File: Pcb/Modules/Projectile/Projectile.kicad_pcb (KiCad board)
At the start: 2 copper layers, 55.2 x 20.2 mm, 18 parts, among them J1 Conn_01x02, J2 Conn_01x04, Q1 BC817, U1 OP249

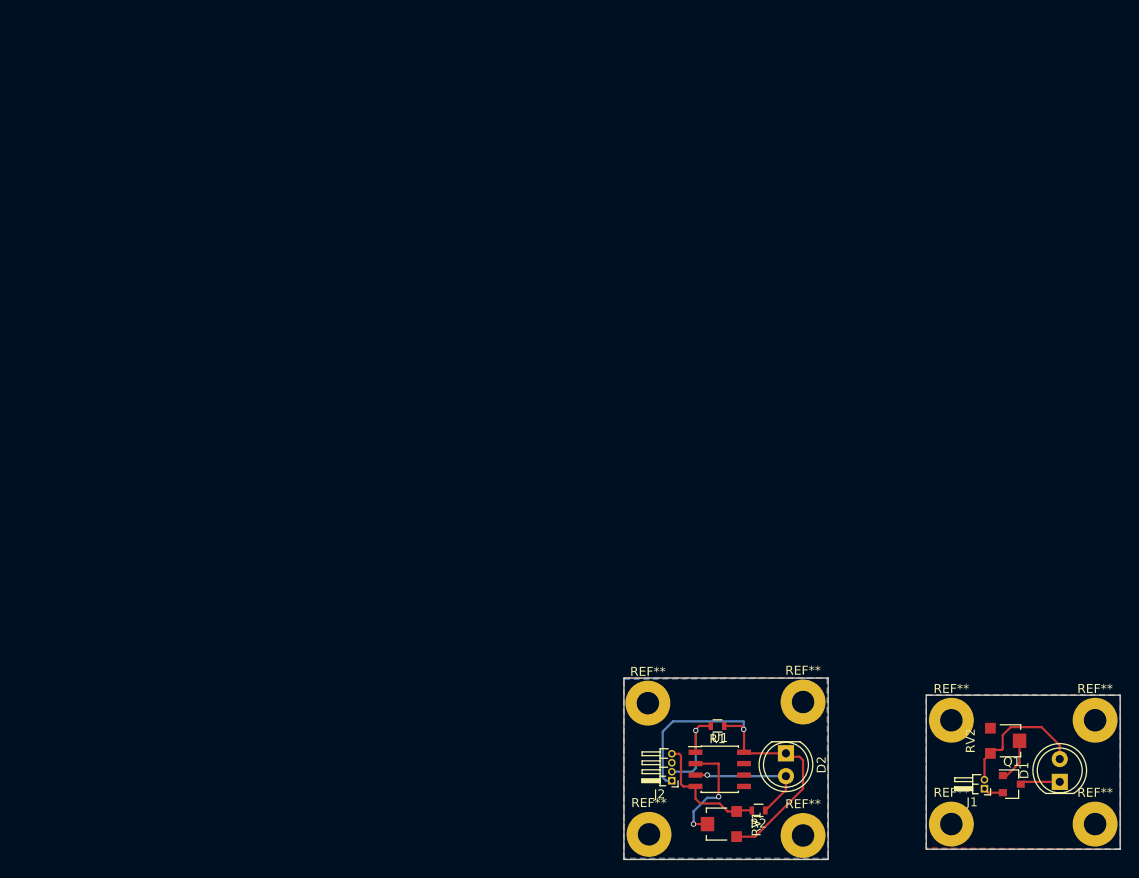
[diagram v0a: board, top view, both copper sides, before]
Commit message: Pcb layout for beam and projectile module
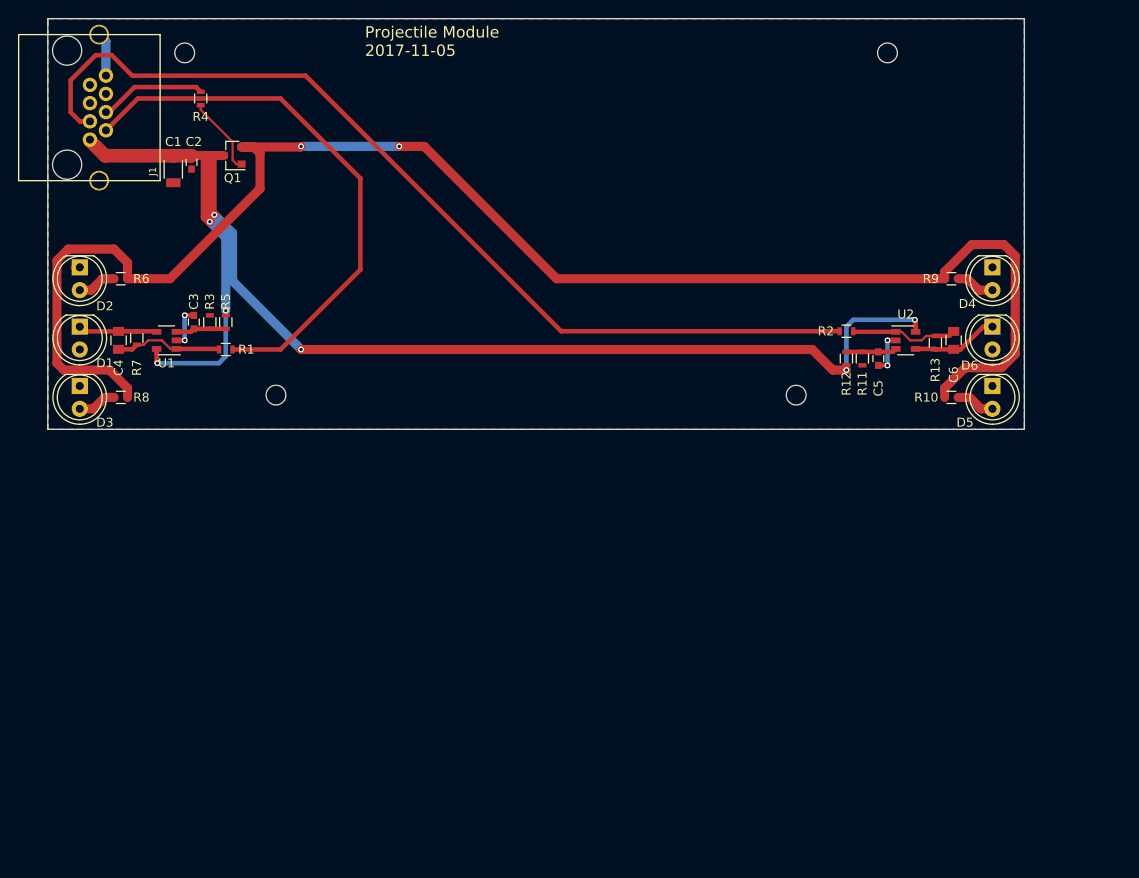
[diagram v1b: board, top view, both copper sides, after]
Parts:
- removed J2: Conn_01x04, Pin_Headers:Pin_Header_Angled_1x04_Pitch1.00mm
- removed REF** (x8): MountingHole_2.5mm_Pad, Mounting_Holes:MountingHole_2.5mm_Pad
- removed RV1, RV2: POT, Potentiometers:Potentiometer_Trimmer-EVM3E
- added C1: 10uF, Capacitors_SMD:C_1206, F.Cu at (43.2, 40.9)
- added C2: 0.1uF, Capacitors_SMD:C_0603, F.Cu at (45.2, 40.1)
- added C3: 1uF, Capacitors_SMD:C_0603, F.Cu at (45.5, 57.9)
- added C4: 4.3pF, Capacitors_SMD:C_0805, F.Cu at (37.1, 59.9)
- added C5: 1uF, Capacitors_SMD:C_0603, F.Cu at (121.7, 62.0)
- added C6: 4.3pF, Capacitors_SMD:C_0805, F.Cu at (130.0, 59.9)
- added D3: LED, LEDs:LED_D5.0mm, F.Cu at (32.8, 65.0)
- added D4: LED, LEDs:LED_D5.0mm, F.Cu at (134.4, 51.8)
- added D5: LED, LEDs:LED_D5.0mm, F.Cu at (134.4, 65.0)
- added D6: D_Photo, LEDs:LED_D5.0mm, F.Cu at (134.4, 58.4)
- added R10: 30R, Resistors_SMD:R_0603, F.Cu at (129.8, 66.3)
- added R11: 8.98K, Resistors_SMD:R_0603, F.Cu at (119.9, 62.0)
- added R12: 280R, Resistors_SMD:R_0603, F.Cu at (118.1, 62.0)
- added R13: 34.8K, Resistors_SMD:R_0603, F.Cu at (128.0, 60.2)
- added R3: 8.98K, Resistors_SMD:R_0603, F.Cu at (47.2, 57.9)
- added R4: 1K, Resistors_SMD:R_0603, F.Cu at (46.2, 33.0)
- added R5: 280R, Resistors_SMD:R_0603, F.Cu at (49.0, 57.9)
- added R6: 30R, Resistors_SMD:R_0603, F.Cu at (37.3, 53.1)
- added R7: 34.8K, Resistors_SMD:R_0603, F.Cu at (39.1, 59.7)
- added R8: 30R, Resistors_SMD:R_0603, F.Cu at (37.3, 66.3)
- added R9: 30R, Resistors_SMD:R_0603, F.Cu at (129.8, 53.1)
- added U2: OPA320, TO_SOT_Packages_SMD:SOT-23-5, F.Cu at (124.7, 59.9)
- added X1: HOLE, Mounting_Holes:MountingHole_2.2mm_M2, F.Cu at (112.5, 66.0)
- added X2: HOLE, Mounting_Holes:MountingHole_2.2mm_M2, F.Cu at (54.6, 66.0)
- added X3: HOLE, Mounting_Holes:MountingHole_2.2mm_M2, F.Cu at (44.5, 27.9)
- added X4: HOLE, Mounting_Holes:MountingHole_2.2mm_M2, F.Cu at (122.7, 27.9)
- D1: value LD274 -> D_Photo
- D2: value LD274 -> LED
- J1: value Conn_01x02 -> JACK_RJ45; footprint Pin_Headers:Pin_Header_Angled_1x02_Pitch1.00mm -> CA6:RJ45_pcbwing
- Q1: value BC817 -> Q_NMOS_GSD
- R1, R2: value R -> 50R
- U1: value OP249 -> OPA320; footprint Housings_SOIC:SOIC-8_3.9x4.9mm_Pitch1.27mm -> TO_SOT_Packages_SMD:SOT-23-5
- moved J1 125.3 mm to (33.8, 34.0), turned to 270 degrees
- moved D1 120.3 mm to (32.8, 58.4), turned to 270 degrees
- moved Q1 111.4 mm to (49.8, 39.4), turned to 180 degrees
- moved D2 95.4 mm to (32.8, 51.8)
- moved U1 77.9 mm to (42.4, 59.9), turned to 180 degrees
- moved R1 68.9 mm to (49.0, 61.0), turned to 0 degrees
- moved R2 54.2 mm to (118.1, 58.9)
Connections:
- D1 pad 1: Net-(D1-Pad1) -> Net-(C4-Pad2)
- D1 pad 2: Net-(D1-Pad2) -> GND
- D2 pad 1: Net-(D2-Pad1) -> GND
- J1 pad 1: Net-(J1-Pad1) -> 3V3
- J1 pad 2: Net-(D1-Pad2) -> Net-(J1-Pad2)
- Q1 pad 2: Net-(J1-Pad1) -> Net-(Q1-Pad2)
- Q1 pad 3: Net-(D1-Pad1) -> 3V3
- R1 pad 1: Net-(D2-Pad1) -> Net-(C4-Pad1)
- R1 pad 2: Net-(J2-Pad2) -> Net-(J1-Pad2)
- R2 pad 1: Net-(D2-Pad2) -> Net-(C6-Pad1)
- R2 pad 2: Net-(J2-Pad4) -> Net-(J1-Pad3)
- U1 pad 1: Net-(J2-Pad2) -> Net-(C4-Pad1)
- U1 pad 2: Net-(RV1-Pad2) -> GND
- U1 pad 3: Net-(D2-Pad2) -> Net-(C3-Pad1)
- U1 pad 4: Net-(J2-Pad4) -> Net-(C4-Pad2)
- U1 pad 5: (no net) -> 3V3
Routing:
- net Net-(Q1-Pad2): track 0.00 -> 173.6 mm, vias 0 -> 2
- net 3V3: track 0.00 -> 151.1 mm, vias 0 -> 7
- net Net-(J1-Pad3): track 0.00 -> 105.6 mm
- net Net-(J1-Pad2): track 0.00 -> 61.6 mm
- net Net-(D2-Pad1): track 41.4 -> 0.00 mm, vias 1 -> 0
- net Net-(D1-Pad2): track 15.4 -> 0.00 mm
- net GND: track 0.00 -> 14.9 mm, vias 0 -> 4
- net Net-(J2-Pad4): track 14.3 -> 0.00 mm
- net Net-(RV1-Pad2): track 12.7 -> 0.00 mm, vias 2 -> 0
- net Net-(C6-Pad1): track 0.00 -> 12.0 mm
- net Net-(C4-Pad1): track 0.00 -> 12.0 mm
- net Net-(J1-Pad4): track 0.00 -> 11.9 mm
- net Net-(J2-Pad2): track 11.5 -> 0.00 mm, vias 1 -> 0
- net Net-(D2-Pad2): track 14.9 -> 4.35 mm, vias 1 -> 0
- net Net-(C6-Pad2): track 0.00 -> 9.62 mm
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- added copper zone on B.Cu, net GND
- added copper zone on F.Cu, net GND
- removed copper zone on B.Cu, net (none)
- removed copper zone on F.Cu, net (none)
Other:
- board size 55.2 x 20.2 mm -> 108.7 x 45.7 mm
- net class Default: clearance 0.2 -> 0.2032; trace_width 0.25 -> 0.254; via_dia 0.6 -> 0.6604; via_drill 0.4 -> 0.3556
- rule trace_clearance: 0.2 -> 0.2032
- board text added: "Projectile Module 2017-11-05"

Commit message: Change 50 ohm resistor to 49.9
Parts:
- R1, R2: value 50R -> 49.9R
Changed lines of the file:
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@@
       (effects (font (size 1 1) (thickness 0.15)))
     )
-    (fp_text value 50R (at 0 1.5) (layer F.Fab) hide
+    (fp_text value 49.9R (at 0 1.5) (layer F.Fab) hide
       (effects (font (size 1 1) (thickness 0.15)))
     )
@@
       (effects (font (size 1 1) (thickness 0.15)))
     )
-    (fp_text value 50R (at 0 1.5 180) (layer F.Fab) hide
+    (fp_text value 49.9R (at 0 1.5 180) (layer F.Fab) hide
       (effects (font (size 1 1) (thickness 0.15)))
     )

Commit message: Update PCBs
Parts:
- added R14: 100K, Resistors_SMD:R_0603, F.Cu at (49.8, 42.7)
- J1: moved to B.Cu
- R10, R6, R8, R9: value 30R -> 49.9
- R11, R3: value 8.98K -> 280R
- R12, R5: value 280R -> 8.98K
- R13, R7: value 34.8K -> 100K
- X1, X2, X3, X4: footprint Mounting_Holes:MountingHole_2.2mm_M2 -> Mounting_Holes:MountingHole_2.5mm_Pad
- moved X4 10.3 mm to (112.4, 27.9)
- moved X3 10.2 mm to (54.6, 27.9)
- moved R4 4.05 mm to (48.9, 36.1), turned to 0 degrees
- moved X1 0.13 mm to (112.4, 66.0)
- turned J1 to 90 degrees
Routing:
- net 3V3: track 151.1 -> 162.3 mm
- net Net-(J1-Pad3): track 105.6 -> 101.4 mm, vias 0 -> 1
- net GND: track 14.9 -> 11.4 mm, vias 4 -> 5
- net Net-(J1-Pad4): track 11.9 -> 13.5 mm
- net Net-(Q1-Pad1): track 8.76 -> 7.18 mm
- net Net-(J1-Pad2): track 61.6 -> 60.7 mm
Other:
- board text added: "Projectile Module 2017-12-03"
- board text removed: "Projectile Module 2017-11-05"

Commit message: Update pcbs.
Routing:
- net GND: track 11.4 -> 17.2 mm, vias 5 -> 10
- removed copper zone on F.Cu, net GND
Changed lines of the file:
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@@
     (thickness 1.6)
     (drawings 5)
-    (tracks 167)
+    (tracks 179)
     (zones 0)
     (modules 34)
@@
   )
   (setup
-    (last_trace_width 0.508)
+    (last_trace_width 0.254)
     (user_trace_width 0.2032)
     (user_trace_width 0.254)
@@
       (effects (font (size 1 1) (thickness 0.15)))
     )
-    (fp_text value D_Photo (at 1.27 3.96 270) (layer F.Fab)
+    (fp_text value D_Photo (at 1.27 3.96 270) (layer F.Fab) hide
       (effects (font (size 1 1) (thickness 0.15)))
     )
@@
       (effects (font (size 1 1) (thickness 0.15)))
     )
-    (fp_text value LED (at 1.27 3.96 270) (layer F.Fab)
+    (fp_text value LED (at 1.27 3.96 270) (layer F.Fab) hide
       (effects (font (size 1 1) (thickness 0.15)))
     )
@@
       (effects (font (size 1 1) (thickness 0.15)))
     )
-    (fp_text value LED (at 1.27 3.96 270) (layer F.Fab)
+    (fp_text value LED (at 1.27 3.96 270) (layer F.Fab) hide
       (effects (font (size 1 1) (thickness 0.15)))
     )
@@
       (effects (font (size 1 1) (thickness 0.15)))
     )
-    (fp_text value LED (at 1.27 3.96 270) (layer F.Fab)
+    (fp_text value LED (at 1.27 3.96 270) (layer F.Fab) hide
       (effects (font (size 1 1) (thickness 0.15)))
     )
@@
       (effects (font (size 1 1) (thickness 0.15)))
     )
-    (fp_text value LED (at 1.27 3.96 270) (layer F.Fab)
+    (fp_text value LED (at 1.27 3.96 270) (layer F.Fab) hide
       (effects (font (size 1 1) (thickness 0.15)))
     )
@@
       (effects (font (size 1 1) (thickness 0.15)))
     )
-    (fp_text value D_Photo (at 1.27 3.96 270) (layer F.Fab)
+    (fp_text value D_Photo (at 1.27 3.96 270) (layer F.Fab) hide
       (effects (font (size 1 1) (thickness 0.15)))
     )
@@
       (effects (font (size 1 1) (thickness 0.15)))
     )
-    (fp_text value 49.9 (at 0 1.5) (layer F.Fab)
+    (fp_text value 49.9 (at 0 1.5) (layer F.Fab) hide
       (effects (font (size 1 1) (thickness 0.15)))
     )
@@
       (effects (font (size 1 1) (thickness 0.15)))
     )
-    (fp_text value 49.9 (at 0 1.5) (layer F.Fab)
+    (fp_text value 49.9 (at 0 1.5) (layer F.Fab) hide
       (effects (font (size 1 1) (thickness 0.15)))
     )
@@
       (effects (font (size 1 1) (thickness 0.15)))
     )
-    (fp_text value 49.9 (at 0 1.5 180) (layer F.Fab)
+    (fp_text value 49.9 (at 0 1.5 180) (layer F.Fab) hide
       (effects (font (size 1 1) (thickness 0.15)))
     )
@@
   (segment (start 41.318 62.4) (end 41.402 62.484) (width 0.508) (layer F.Cu) (net 1))
   (segment (start 41.318 60.894) (end 41.318 62.4) (width 0.508) (layer F.Cu) (net 1) (status 10))
-  (segment (start 49.034 42.672) (end 49.034 41.795) (width 0.508) (layer F.Cu) (net 2))
-  (via (at 48.641 41.402) (size 0.6604) (drill 0.3556) (layers F.Cu B.Cu) (net 2))
-  (segment (start 49.034 41.795) (end 48.641 41.402) (width 0.508) (layer F.Cu) (net 2))
+  (segment (start 43.18 42.394) (end 43.18 43.688) (width 1.016) (layer F.Cu) (net 2))
+  (via (at 43.18 43.688) (size 0.6604) (drill 0.3556) (layers F.Cu B.Cu) (net 2))
+  (segment (start 43.18 42.394) (end 41.426 42.394) (width 1.016) (layer F.Cu) (net 2))
+  (via (at 41.148 42.672) (size 0.6604) (drill 0.3556) (layers F.Cu B.Cu) (net 2))
+  (segment (start 41.426 42.394) (end 41.148 42.672) (width 1.016) (layer F.Cu) (net 2))
+  (segment (start 49.034 42.672) (end 49.034 41.668) (width 0.508) (layer F.Cu) (net 2))
+  (via (at 49.022 41.656) (size 0.6604) (drill 0.3556) (layers F.Cu B.Cu) (net 2))
+  (segment (start 49.034 41.668) (end 49.022 41.656) (width 0.508) (layer F.Cu) (net 2))
+  (segment (start 45.212 40.882) (end 45.212 41.91) (width 0.508) (layer F.Cu) (net 2))
+  (via (at 45.212 41.91) (size 0.6604) (drill 0.3556) (layers F.Cu B.Cu) (net 2))
+  (segment (start 47.244 57.162) (end 47.002 57.162) (width 0.508) (layer F.Cu) (net 2))
+  (segment (start 47.002 57.162) (end 46.482 56.642) (width 0.508) (layer F.Cu) (net 2))
+  (via (at 46.482 56.642) (size 0.6604) (drill 0.3556) (layers F.Cu B.Cu) (net 2))
+  (segment (start 119.888 62.726) (end 119.888 63.5) (width 0.508) (layer F.Cu) (net 2))
+  (via (at 119.888 63.5) (size 0.6604) (drill 0.3556) (layers F.Cu B.Cu) (net 2))
   (segment (start 123.614 59.944) (end 122.682 59.944) (width 0.508) (layer F.Cu) (net 2) (status 10))
   (segment (start 122.67 62.726) (end 121.666 62.726) (width 0.508) (layer F.Cu) (net 2) (status 20))
@@
   (segment (start 52.832 43.053) (end 52.832 39.116) (width 1.016) (layer F.Cu) (net 17))
   (segment (start 42.799 53.086) (end 52.832 43.053) (width 1.016) (layer F.Cu) (net 17))
-  (zone (net 2) (net_name GND) (layer F.Cu) (hatch edge 0.508)
-    (connect_pads (clearance 0.254))
-    (min_thickness 0.3048)
-    (fill yes (arc_segments 16) (thermal_gap 0.1524) (thermal_bridge_width 0.381))
-    (polygon
-      (pts
-        (xy 137.922 69.85) (xy 29.21 69.85) (xy 29.21 24.13) (xy 137.922 24.13)
-      )
-    )
-  )
   (zone (net 2) (net_name GND) (layer B.Cu) (hatch edge 0.508)
     (connect_pads (clearance 0.254))

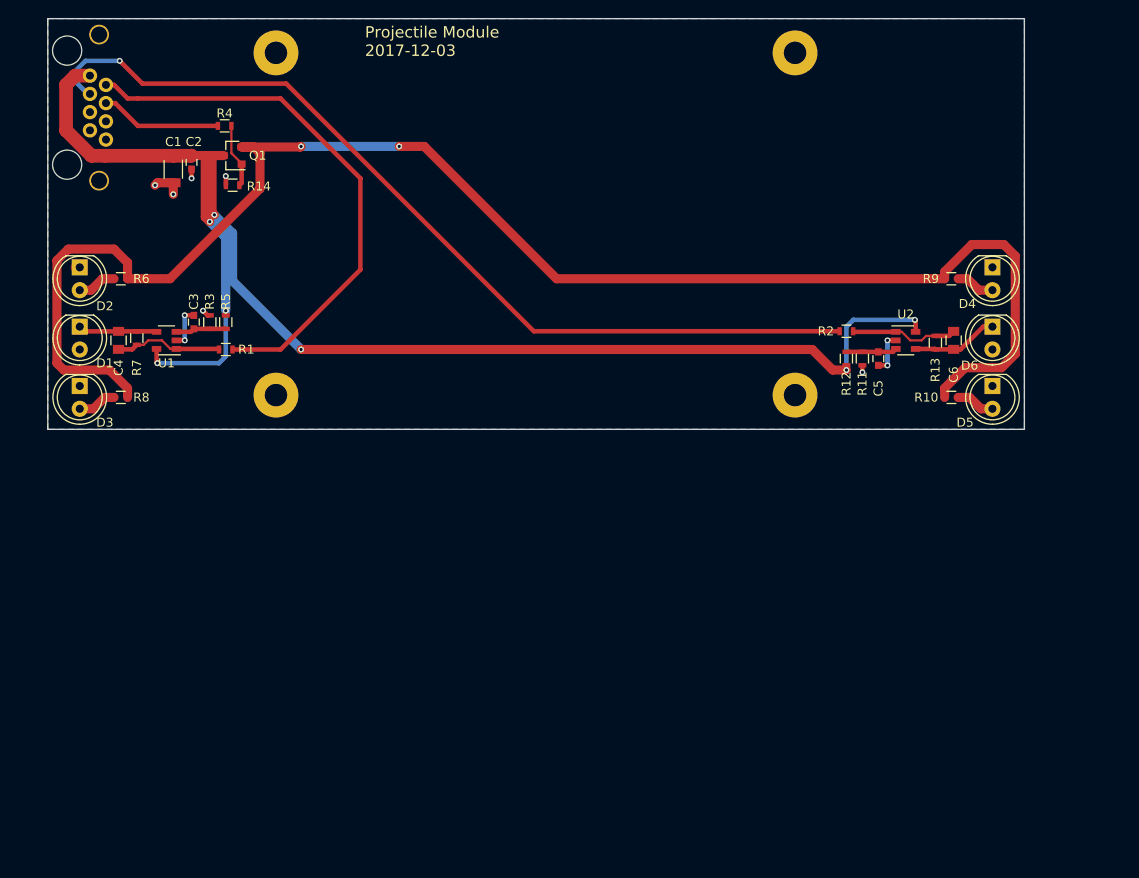
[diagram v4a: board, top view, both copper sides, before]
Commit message: Update PCBs to use n channel mosfet on low side
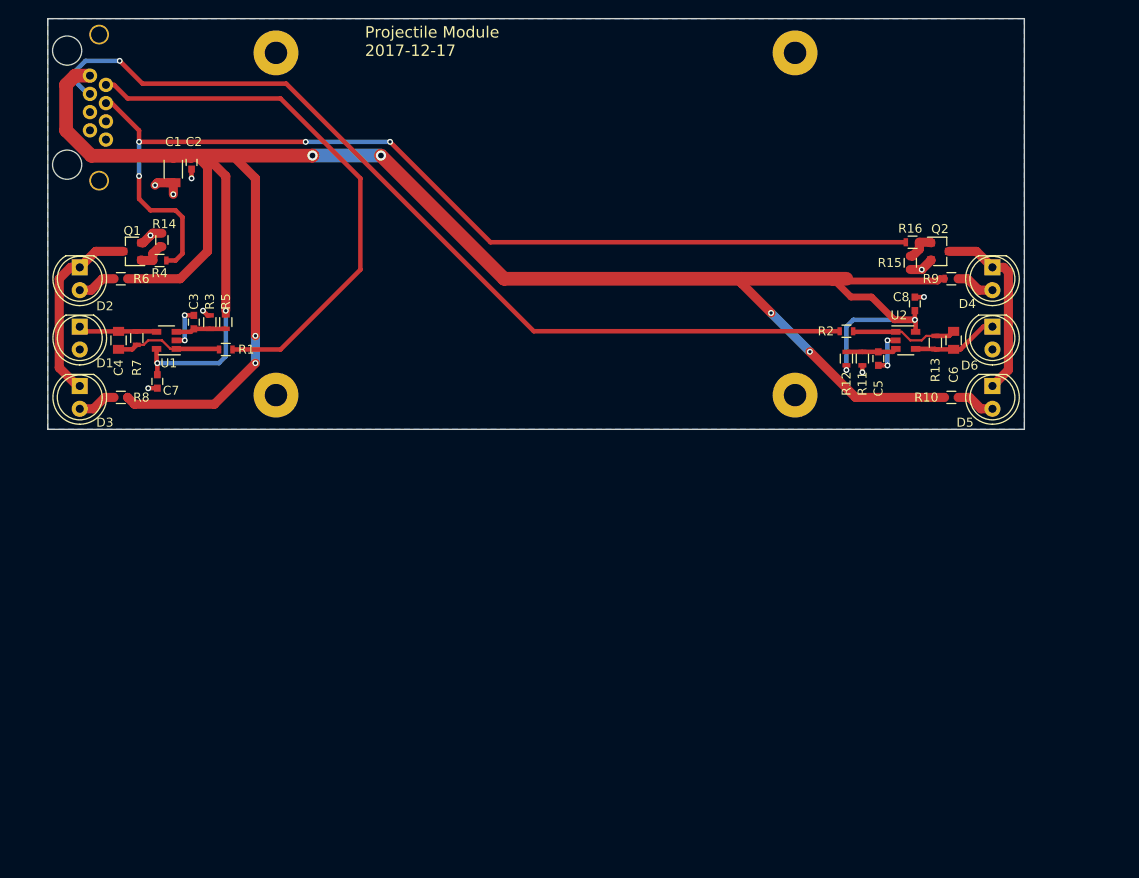
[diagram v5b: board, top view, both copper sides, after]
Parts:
- added C7: 0.1uF, Capacitors_SMD:C_0603, F.Cu at (41.4, 64.5)
- added C8: 0.1uF, Capacitors_SMD:C_0603, F.Cu at (125.7, 55.9)
- added Q2: Q_NMOS_GSD, TO_SOT_Packages_SMD:SOT-23, F.Cu at (128.5, 50.0)
- added R15: 100K, Resistors_SMD:R_0603, F.Cu at (125.2, 51.3)
- added R16: 1K, Resistors_SMD:R_0603, F.Cu at (125.5, 49.0)
- moved R4 16.6 mm to (41.7, 51.1), turned to 180 degrees
- moved Q1 15.5 mm to (38.6, 50.0)
- moved R14 9.96 mm to (41.9, 48.8), turned to 90 degrees
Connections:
- D2 pad 1: GND -> Net-(D2-Pad1)
- D3 pad 1: GND -> Net-(D2-Pad1)
- D4 pad 1: GND -> Net-(D4-Pad1)
- D5 pad 1: GND -> Net-(D4-Pad1)
- Q1 pad 2: Net-(Q1-Pad2) -> GND
- Q1 pad 3: 3V3 -> Net-(D2-Pad1)
- R10 pad 2: Net-(Q1-Pad2) -> 3V3
- R6 pad 2: Net-(Q1-Pad2) -> 3V3
- R8 pad 2: Net-(Q1-Pad2) -> 3V3
- R9 pad 2: Net-(Q1-Pad2) -> 3V3
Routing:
- net Net-(Q1-Pad2): track 173.6 -> 0.00 mm, vias 2 -> 0
- net 3V3: track 162.3 -> 270.9 mm, vias 7 -> 10
- net Net-(J1-Pad4): track 13.5 -> 114.4 mm, vias 0 -> 4
- net Net-(D2-Pad1): track 0.00 -> 21.9 mm
- net Net-(D4-Pad1): track 0.00 -> 21.0 mm
- net GND: track 17.2 -> 23.3 mm, vias 10 -> 13
- net Net-(Q1-Pad1): track 7.18 -> 3.42 mm
- net Net-(Q2-Pad1): track 0.00 -> 3.42 mm
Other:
- board text added: "Projectile Module 2017-12-17"
- board text removed: "Projectile Module 2017-12-03"

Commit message: Change 100K to 10K resistors
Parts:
- R14, R15: value 100K -> 10K
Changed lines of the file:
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@@
   )
   (setup
-    (last_trace_width 0.762)
+    (last_trace_width 0.254)
     (user_trace_width 0.2032)
     (user_trace_width 0.254)
@@
       (effects (font (size 1 1) (thickness 0.15)))
     )
-    (fp_text value 100K (at 0 1.5 90) (layer F.Fab) hide
+    (fp_text value 10K (at 0 1.5 90) (layer F.Fab) hide
       (effects (font (size 1 1) (thickness 0.15)))
     )
@@
       (effects (font (size 1 1) (thickness 0.15)))
     )
-    (fp_text value 100K (at 0 1.5 270) (layer F.Fab) hide
-      (effects (font (size 1 1) (thickness 0.15)))
-    )
+    (fp_text value 10K (at 0 1.5 270) (layer F.Fab) hide
+      (effects (font (size 1 1) (thickness 0.15)))
+    )

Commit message: Update CA6 PCB.  Also update versions of all the module pcbs to match.
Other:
- board text added: "Projectile Module 2017.12.23"
- board text removed: "Projectile Module 2017-12-17"
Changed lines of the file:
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@@
     (links 64)
     (no_connects 0)
-    (area 29.134999 24.054999 137.997001 69.925001)
+    (area 25.683869 23.4618 137.997001 70.6182)
     (thickness 1.6)
     (drawings 5)
@@
   (gr_line (start 137.922 24.13) (end 29.21 24.13) (angle 90) (layer Edge.Cuts) (width 0.15))
   (gr_line (start 29.21 69.85) (end 137.922 69.85) (angle 90) (layer Edge.Cuts) (width 0.15))
-  (gr_text "Projectile Module\n2017-12-17" (at 64.516 26.67) (layer F.SilkS)
+  (gr_text "Projectile Module\n2017.12.23" (at 64.516 26.67) (layer F.SilkS)
     (effects (font (size 1.27 1.27) (thickness 0.254)) (justify left))
   )
